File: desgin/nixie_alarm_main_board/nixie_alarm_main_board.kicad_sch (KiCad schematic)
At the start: 1 part, among them U1 ESP32-S3-WROOM-1

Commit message: copper border
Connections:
- net ENC_A: now also U1.38 (IO2); no longer U1.39 (IO1)
- net ENC_B: now also U1.39 (IO1); no longer U1.38 (IO2)

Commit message: little fixes
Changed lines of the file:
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@@
 	)
 	(sheet
-		(at 82.042 145.796)
-		(size 30.48 12.7)
+		(at 83.566 62.738)
+		(size 30.48 8.128)
 		(fields_autoplaced yes)
 		(stroke
@@
 		)
 		(property "Sheetname" "Debug_UART"
-			(at 82.042 145.0844 0)
+			(at 83.566 62.0264 0)
 			(effects
 				(font
@@
 		)
 		(property "Sheetfile" "Debug_UART.kicad_sch"
-			(at 82.042 159.0806 0)
+			(at 83.566 71.4506 0)
 			(effects
 				(font

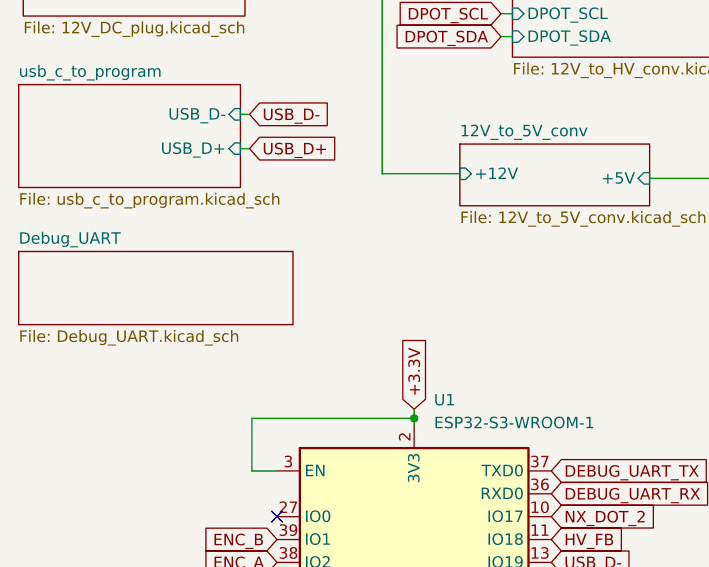
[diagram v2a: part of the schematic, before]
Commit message: tvs added
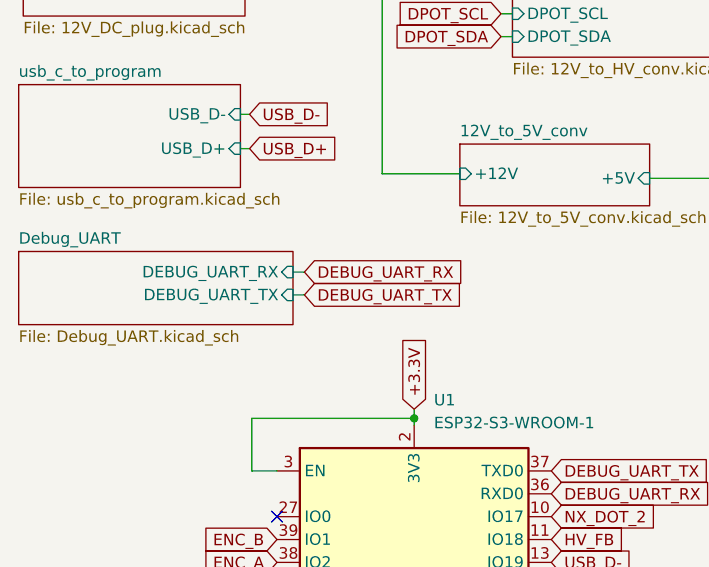
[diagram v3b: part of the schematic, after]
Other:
- sheet Debug_UART ports: added DEBUG_UART_RX, DEBUG_UART_TX; removed none
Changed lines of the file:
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@@
+	(wire
+		(pts
+			(xy 114.046 65.024) (xy 115.316 65.024)
+		)
+		(stroke
+			(width 0)
+			(type default)
+		)
+	)
 	(wire
 		(pts
@@
 	(wire
 		(pts
+			(xy 114.046 67.564) (xy 115.316 67.564)
+		)
+		(stroke
+			(width 0)
+			(type default)
+		)
+	)
+	(wire
+		(pts
 			(xy 190.754 81.28) (xy 191.77 81.28)
 		)
@@
 		)
 	)
+	(global_label "DEBUG_UART_RX"
+		(shape input)
+		(at 115.316 65.024 0)
+		(fields_autoplaced yes)
+		(effects
+			(font
+				(size 1.27 1.27)
+			)
+			(justify left)
+		)
+		(property "Intersheetrefs" "${INTERSHEET_REFS}"
+			(at 133.6621 65.024 0)
+			(effects
+				(font
+					(size 1.27 1.27)
+				)
+				(justify left)
+				(hide yes)
+			)
+		)
+	)
 	(global_label "NX_DOT_6"
 		(shape input)
@@
 				)
 				(justify right)
+				(hide yes)
+			)
+		)
+	)
+	(global_label "DEBUG_UART_TX"
+		(shape input)
+		(at 115.316 67.564 0)
+		(fields_autoplaced yes)
+		(effects
+			(font
+				(size 1.27 1.27)
+			)
+			(justify left)
+		)
+		(property "Intersheetrefs" "${INTERSHEET_REFS}"
+			(at 133.3597 67.564 0)
+			(effects
+				(font
+					(size 1.27 1.27)
+				)
+				(justify left)
 				(hide yes)
 			)
@@
 			)
 		)
+		(pin "DEBUG_UART_RX" input
+			(at 114.046 65.024 0)
+			(effects
+				(font
+					(size 1.27 1.27)
+				)
+				(justify right)
+			)
+		)
+		(pin "DEBUG_UART_TX" input
+			(at 114.046 67.564 0)
+			(effects
+				(font
+					(size 1.27 1.27)
+				)
+				(justify right)
+			)
+		)

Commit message: fixes added
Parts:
- added C28: 100nF 25V, Capacitor_SMD:C_0805_2012Metric_Pad1.18x1.45mm_HandSolder, symbol SamacSys_Parts:GRM033R71E101KA01J
- added H1, H2, H3, H4: MountingHole_Pad, MountingHole:MountingHole_3.2mm_M3_Pad_Via, symbol Mechanical:MountingHole_Pad
- added TP1: +3.3V, TestPoint:TestPoint_Pad_D2.0mm, symbol Connector:TestPoint
- added TP2: +5V, TestPoint:TestPoint_Pad_D2.0mm, symbol Connector:TestPoint
- added TP3: +12V, TestPoint:TestPoint_Pad_D2.0mm, symbol Connector:TestPoint
- added TP4: +HV, TestPoint:TestPoint_Pad_D2.0mm, symbol Connector:TestPoint
- added TP5: GND, TestPoint:TestPoint_Pad_D2.0mm, symbol Connector:TestPoint
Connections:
- net +12V: now also TP3.1
- net +3.3V: now also C28.1, TP1.1
- net +5V: now also TP2.1
- net GND: now also C28.2, H1.1, H2.1, H3.1, H4.1, TP5.1
- net HV: now also TP4.1

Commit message: final fixes
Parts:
- renumbered TP3 to +12V1, TP1 to +3.3V1, TP2 to +5V1, TP4 to +HV1, TP5 to GND1
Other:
- note added: "TEST PADS"
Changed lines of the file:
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@@
+		)
+	)
+	(text "TEST PADS"
+		(exclude_from_sim no)
+		(at 86.106 122.682 0)
+		(effects
+			(font
+				(size 1.27 1.27)
+			)
 		)
 	)
@@
 		)
 		(instances
-			(project ""
+			(project "nixie_alarm_main_board"
 				(path "/a0d555d7-39a0-4a98-b831-70d97d0aa5a1"
 					(reference "H1")
@@
 		(on_board yes)
 		(dnp no)
-		(fields_autoplaced yes)
-		(property "Reference" "TP4"
-			(at 85.598 147.32 90)
+		(property "Reference" "+HV1"
+			(at 85.09 150.368 90)
 			(effects
 				(font
@@
 					(size 1.27 1.27)
 				)
+				(hide yes)
 			)
 		)
@@
 			(project "nixie_alarm_main_board"
 				(path "/a0d555d7-39a0-4a98-b831-70d97d0aa5a1"
-					(reference "TP4")
+					(reference "+HV1")
 					(unit 1)
 				)
@@
 		(dnp no)
 		(fields_autoplaced yes)
-		(property "Reference" "TP5"
-			(at 85.598 154.94 90)
+		(property "Reference" "GND1"
+			(at 85.598 157.48 90)
 			(effects
 				(font
@@
 					(size 1.27 1.27)
 				)
+				(hide yes)
 			)
 		)
@@
 			(project "nixie_alarm_main_board"
 				(path "/a0d555d7-39a0-4a98-b831-70d97d0aa5a1"
-					(reference "TP5")
+					(reference "GND1")
 					(unit 1)
 				)
@@
 		(on_board yes)
 		(dnp no)
-		(fields_autoplaced yes)
-		(property "Reference" "TP1"
-			(at 85.598 124.46 90)
+		(property "Reference" "+3.3V1"
+			(at 85.09 127 90)
 			(effects
 				(font
@@
 					(size 1.27 1.27)
 				)
+				(hide yes)
 			)
 		)
@@
 		)
 		(instances
-			(project ""
+			(project "nixie_alarm_main_board"
 				(path "/a0d555d7-39a0-4a98-b831-70d97d0aa5a1"
-					(reference "TP1")
+					(reference "+3.3V1")
 					(unit 1)
 				)
@@
 		(on_board yes)
 		(dnp no)
-		(fields_autoplaced yes)
-		(property "Reference" "TP3"
-			(at 85.598 139.7 90)
+		(property "Reference" "+12V1"
+			(at 85.09 142.748 90)
 			(effects
 				(font
@@
 					(size 1.27 1.27)
 				)
+				(hide yes)
 			)
 		)
@@
 			(project "nixie_alarm_main_board"
 				(path "/a0d555d7-39a0-4a98-b831-70d97d0aa5a1"
-					(reference "TP3")
+					(reference "+12V1")
 					(unit 1)
 				)
@@
 		(on_board yes)
 		(dnp no)
-		(fields_autoplaced yes)
-		(property "Reference" "TP2"
-			(at 85.598 132.08 90)
+		(property "Reference" "+5V1"
+			(at 85.344 134.874 90)
 			(effects
 				(font
@@
 					(size 1.27 1.27)
 				)
+				(hide yes)
 			)
 		)
@@
 			(project "nixie_alarm_main_board"
 				(path "/a0d555d7-39a0-4a98-b831-70d97d0aa5a1"
-					(reference "TP2")
+					(reference "+5V1")
 					(unit 1)
 				)

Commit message: marged with board v2
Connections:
- net +3.3V: no longer U1.3 (EN)
- net buttons/SW_GPIO0: now reaches U1.27 (IO0)
- new net buttons/SW_EN: U1.3 (EN)
- no-connect marks 9 -> 8
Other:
- added sheet buttons (buttons.kicad_sch)
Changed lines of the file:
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@@
-		(color 0 0 0 0)
-	)
-	(junction
-		(at 109.474 81.28)
-		(diameter 0)
 		(color 0 0 0 0)
 	)
@@
 	)
 	(no_connect
-		(at 112.268 92.202)
-	)
-	(no_connect
 		(at 142.748 122.682)
 	)
@@
 	(wire
 		(pts
-			(xy 109.474 81.28) (xy 127.508 81.28)
+			(xy 109.22 81.28) (xy 127.508 81.28)
 		)
 		(stroke
@@
 	(wire
 		(pts
-			(xy 109.474 87.122) (xy 109.474 81.28)
-		)
-		(stroke
-			(width 0)
-			(type default)
-		)
-	)
-	(wire
-		(pts
 			(xy 190.754 85.09) (xy 191.77 85.09)
 		)
@@
 	(wire
 		(pts
+			(xy 112.268 92.202) (xy 83.566 92.202)
+		)
+		(stroke
+			(width 0)
+			(type default)
+		)
+	)
+	(wire
+		(pts
 			(xy 153.67 54.61) (xy 165.862 54.61)
 		)
@@
 	(wire
 		(pts
+			(xy 83.566 87.122) (xy 112.268 87.122)
+		)
+		(stroke
+			(width 0)
+			(type default)
+		)
+	)
+	(wire
+		(pts
 			(xy 123.19 153.67) (xy 128.27 153.67)
 		)
@@
 	(wire
 		(pts
-			(xy 109.22 81.28) (xy 109.474 81.28)
-		)
-		(stroke
-			(width 0)
-			(type default)
-		)
-	)
-	(wire
-		(pts
 			(xy 190.754 77.47) (xy 191.77 77.47)
 		)
@@
 		(pts
 			(xy 169.926 33.528) (xy 179.832 33.528)
-		)
-		(stroke
-			(width 0)
-			(type default)
-		)
-	)
-	(wire
-		(pts
-			(xy 112.268 87.122) (xy 109.474 87.122)
 		)
 		(stroke
@@
 		(dnp no)
 		(property "Reference" "C28"
-			(at 101.092 85.344 0)
+			(at 100.838 75.184 0)
 			(effects
 				(font
@@
 		)
 		(property "Value" "100nF 25V"
-			(at 97.282 87.122 0)
+			(at 97.028 76.962 0)
 			(effects
 				(font
@@
 				)
 			)
+		)
+	)
+	(sheet
+		(at 60.706 83.82)
+		(size 22.86 11.176)
+		(fields_autoplaced yes)
+		(stroke
+			(width 0.1524)
+			(type solid)
+		)
+		(fill
+			(color 0 0 0 0.0000)
+		)
+		(property "Sheetname" "buttons"
+			(at 60.706 83.1084 0)
+			(effects
+				(font
+					(size 1.27 1.27)
+				)
+				(justify left bottom)
+			)
+		)
+		(property "Sheetfile" "buttons.kicad_sch"
+			(at 60.706 95.5806 0)
+			(effects
+				(font
+					(size 1.27 1.27)
+				)
+				(justify left top)
+			)
+		)
+		(pin "SW_EN" input
+			(at 83.566 87.122 0)
+			(effects
+				(font
+					(size 1.27 1.27)
+				)
+				(justify right)
+			)
+		)
+		(pin "SW_GPIO0" input
+			(at 83.566 92.202 0)
+			(effects
+				(font
+					(size 1.27 1.27)
+				)
+				(justify right)
+			)
+		)
+		(instances
+			(project "nixie_alarm_main_board"
+				(path "/a0d555d7-39a0-4a98-b831-70d97d0aa5a1"
+					(page "12")
+				)
+			)
